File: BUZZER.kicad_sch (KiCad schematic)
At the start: 4 parts, among them Q1 AO3400A, U21 ZX-SH1.0-3PWT

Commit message: update name
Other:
- note removed: "BUZZER"
- company: Pierluigi Colangeli, PhD -> (none)
- title: LEVIA H7 -> (none)

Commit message: upsadte SPI4 set to Baro
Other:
- title: (none) -> H743_ARDUPILOT
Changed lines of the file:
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@@
 	(generator "eeschema")
 	(generator_version "10.0")
-	(paper "A5")
+	(paper "A3")
 	(title_block
+		(title "H743_ARDUPILOT")
 		(date "2026-09-24")
 	)

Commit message: re annotate componant globaly
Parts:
- renumbered R34 to R33, R35 to R34, U21 to U10
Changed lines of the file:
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@@
 		(dnp no)
 		(fields_autoplaced yes)
-		(property "Reference" "#PWR0114"
+		(property "Reference" "#PWR089"
 			(at 135.89 68.58 0)
 			(hide yes)
@@
 			(project "H743_Ardupilot"
 				(path "/6b768b36-fce6-4be0-9021-6d41bddc3a70/40acc3ff-a355-41ce-95b6-fe5d468e4bb9"
-					(reference "#PWR0114")
+					(reference "#PWR089")
 					(unit 1)
 				)
@@
 		(in_pos_files yes)
 		(dnp no)
-		(property "Reference" "R35"
+		(property "Reference" "R34"
 			(at 97.155 64.135 0)
 			(show_name no)
@@
 			(project "H743_Ardupilot"
 				(path "/6b768b36-fce6-4be0-9021-6d41bddc3a70/40acc3ff-a355-41ce-95b6-fe5d468e4bb9"
-					(reference "R35")
+					(reference "R34")
 					(unit 1)
 				)
@@
 		(dnp no)
 		(fields_autoplaced yes)
-		(property "Reference" "#PWR0112"
+		(property "Reference" "#PWR087"
 			(at 104.14 77.47 0)
 			(hide yes)
@@
 			(project "H743_Ardupilot"
 				(path "/6b768b36-fce6-4be0-9021-6d41bddc3a70/40acc3ff-a355-41ce-95b6-fe5d468e4bb9"
-					(reference "#PWR0112")
+					(reference "#PWR087")
 					(unit 1)
 				)
@@
 		(in_pos_files yes)
 		(dnp no)
-		(property "Reference" "R34"
+		(property "Reference" "R33"
 			(at 85.09 60.96 90)
 			(show_name no)
@@
 			(project "H743_Ardupilot"
 				(path "/6b768b36-fce6-4be0-9021-6d41bddc3a70/40acc3ff-a355-41ce-95b6-fe5d468e4bb9"
-					(reference "R34")
+					(reference "R33")
 					(unit 1)
 				)
@@
 		(dnp no)
 		(fields_autoplaced yes)
-		(property "Reference" "#PWR0113"
+		(property "Reference" "#PWR088"
 			(at 133.35 50.8 0)
 			(hide yes)
@@
 			(project "H743_Ardupilot"
 				(path "/6b768b36-fce6-4be0-9021-6d41bddc3a70/40acc3ff-a355-41ce-95b6-fe5d468e4bb9"
-					(reference "#PWR0113")
+					(reference "#PWR088")
 					(unit 1)
 				)
@@
 		(in_pos_files yes)
 		(dnp no)
-		(property "Reference" "U21"
+		(property "Reference" "U10"
 			(at 139.7 45.72 0)
 			(show_name no)
@@
 			(project "H743_Ardupilot"
 				(path "/6b768b36-fce6-4be0-9021-6d41bddc3a70/40acc3ff-a355-41ce-95b6-fe5d468e4bb9"
-					(reference "U21")
+					(reference "U10")
 					(unit 1)
 				)

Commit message: audit DigiKey metadata: BUZZER.kicad_sch
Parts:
- Q1: DigiKey Price Qty (none) -> 1 CT; DigiKey Specs (none) -> N-MOSFET 30 V, 5.7 A, SOT-23-3, RDS(on) 26.5 mΩ max @10 V; DigiKey Status (none) -> Active; DigiKey URL (none) -> https://www.digikey.fr/fr/products/detail/alpha-omega-semic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; DigiKey Unit Price EUR (none) -> 0.45; Footprint Audit (none) -> OK; Library Audit (none) -> KiCad standard; Manufacturer Alpha & Omega Semicon -> Alpha & Omega Semiconductor; Package (none) -> SOT-23-3; Price Checked (none) -> 2026-09-25
- R33: DigiKey Price Qty (none) -> 1 CT; DigiKey Specs (none) -> 1K ±1%, 0402 (1005), thick film; DigiKey Status (none) -> Active / DigiKey family verified; DigiKey URL (none) -> https://www.digikey.fr/en/products/result?keywords=RC0402FR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; DigiKey Unit Price EUR (none) -> 0.09; Footprint Audit (none) -> OK; LCSC C11702 -> (none); LCSC Part C11702 -> (none); Library Audit (none) -> KiCad standard; MPN 0402WGF1001TCE -> RC0402FR-071KL; Manufacturer UNI-ROYAL(Uniroyal Elec) -> YAGEO; Package (none) -> 0402 (1005 Metric); Price Checked (none) -> 2026-09-25
- R34: DigiKey Price Qty (none) -> 1 CT; DigiKey Specs (none) -> 10K ±1%, 0402 (1005), thick film; DigiKey Status (none) -> Active / DigiKey family verified; DigiKey URL (none) -> https://www.digikey.fr/en/products/result?keywords=RC0402FR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; DigiKey Unit Price EUR (none) -> 0.09; Footprint Audit (none) -> OK; LCSC C25744 -> (none); LCSC Part C25744 -> (none); Library Audit (none) -> KiCad standard; MPN 0402WGF1002TCE -> RC0402FR-0710KL; Manufacturer UNI-ROYAL(Uniroyal Elec) -> YAGEO; Package (none) -> 0402 (1005 Metric); Price Checked (none) -> 2026-09-25
- U10: DigiKey Specs (none) -> SH 1.0 mm, 3-pin right-angle SMD; DigiKey Status (none) -> No exact DigiKey listing; supplier/LCSC part retained; Footprint Audit (none) -> CHECK supplier drawing vs EasyEDA footprint; Library Audit (none) -> EasyEDA external; Manufacturer Megastar(兆星) -> Megastar; Package (none) -> SH1.0 3P right-angle SMD; Price Checked (none) -> 2026-09-25

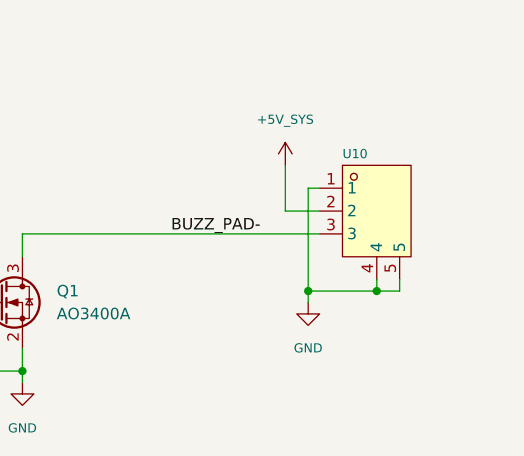
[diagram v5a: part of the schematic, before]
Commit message: add pad for buzzer ouput
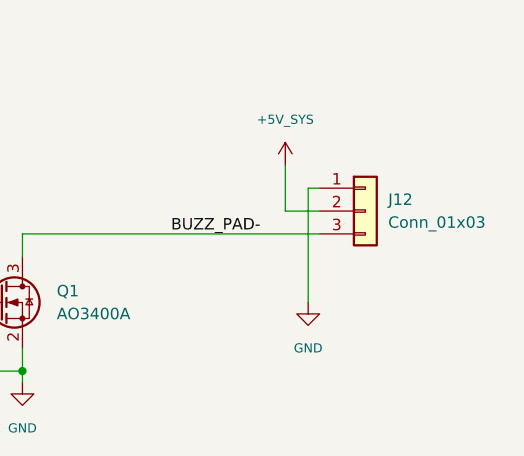
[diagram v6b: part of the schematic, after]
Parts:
- removed U10: ZX-SH1.0-3PWT, EasyEDA:CONN-SMD_3P-P1.00_MEGASTAR_ZX-SH1.0-3PWT, symbol EasyEDA:ZX-SH1.0-3PWT
- added J12: Conn_01x03, symbol Connector_Generic:Conn_01x03
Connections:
- net +5V_SYS: now also J12.2 (Pin_2)
- net BUZZ_PAD-: now also J12.3 (Pin_3)
- net GND: now also J12.1 (Pin_1)
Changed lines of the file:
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@@
 	(generator "eeschema")
 	(generator_version "10.0")
-	(paper "A3")
+	(paper "A4")
 	(title_block
 		(title "H743_ARDUPILOT")
 		(date "2026-09-24")
-	)
-	(junction
-		(at 135.89 60.96)
-		(diameter 0)
-		(color 0 0 0 0)
-	)
-	(junction
-		(at 143.51 60.96)
-		(diameter 0)
-		(color 0 0 0 0)
 	)
 	(junction
@@
 	(wire
 		(pts
-			(xy 143.51 60.96) (xy 146.05 60.96)
-		)
-		(stroke
-			(width 0)
-			(type default)
-		)
-	)
-	(wire
-		(pts
-			(xy 135.89 62.23) (xy 135.89 60.96)
-		)
-		(stroke
-			(width 0)
-			(type default)
-		)
-	)
-	(wire
-		(pts
 			(xy 24.13 33.02) (xy 34.29 33.02)
 		)
@@
 	(wire
 		(pts
-			(xy 143.51 59.69) (xy 143.51 60.96)
-		)
-		(stroke
-			(width 0)
-			(type default)
-		)
-	)
-	(wire
-		(pts
 			(xy 91.44 62.23) (xy 93.98 62.23)
 		)
@@
 	(wire
 		(pts
-			(xy 146.05 60.96) (xy 146.05 59.69)
-		)
-		(stroke
-			(width 0)
-			(type default)
-		)
-	)
-	(wire
-		(pts
 			(xy 135.89 49.53) (xy 137.16 49.53)
 		)
@@
 	(wire
 		(pts
-			(xy 135.89 49.53) (xy 135.89 60.96)
+			(xy 135.89 49.53) (xy 135.89 62.23)
 		)
 		(stroke
@@
 		(pts
 			(xy 93.98 62.23) (xy 93.98 63.5)
-		)
-		(stroke
-			(width 0)
-			(type default)
-		)
-	)
-	(wire
-		(pts
-			(xy 135.89 60.96) (xy 143.51 60.96)
 		)
 		(stroke
@@
 	)
 	(symbol
+		(lib_id "Connector_Generic:Conn_01x03")
+		(at 142.24 52.07 0)
+		(unit 1)
+		(body_style 1)
+		(exclude_from_sim no)
+		(in_bom yes)
+		(on_board yes)
+		(in_pos_files yes)
+		(dnp no)
+		(fields_autoplaced yes)
+		(property "Reference" "J12"
+			(at 144.78 50.7999 0)
+			(show_name no)
+			(do_not_autoplace no)
+			(effects
+				(font
+					(size 1.27 1.27)
+				)
+				(justify left)
+			)
+		)
+		(property "Value" "Conn_01x03"
+			(at 144.78 53.3399 0)
+			(show_name no)
+			(do_not_autoplace no)
+			(effects
+				(font
+					(size 1.27 1.27)
+				)
+				(justify left)
+			)
+		)
+		(property "Footprint" ""
+			(at 142.24 52.07 0)
+			(hide yes)
+			(show_name no)
+			(do_not_autoplace no)
+			(effects
+				(font
+					(size 1.27 1.27)
+				)
+			)
+		)
+		(property "Datasheet" ""
+			(at 142.24 52.07 0)
+			(hide yes)
+			(show_name no)
+			(do_not_autoplace no)
+			(effects
+				(font
+					(size 1.27 1.27)
+				)
+			)
+		)
+		(property "Description" "Generic connector, single row, 01x03, script generated (kicad-library-utils/schlib/autogen/connector/)"
+			(at 142.24 52.07 0)
+			(hide yes)
+			(show_name no)
+			(do_not_autoplace no)
+			(effects
+				(font
+					(size 1.27 1.27)
+				)
+			)
+		)
+		(pin "1"
+		)
+		(pin "2"
+		)
+		(pin "3"
+		)
+		(instances
+			(project "H743_Ardupilot"
+				(path "/6b768b36-fce6-4be0-9021-6d41bddc3a70/40acc3ff-a355-41ce-95b6-fe5d468e4bb9"
+					(reference "J12")
+					(unit 1)
+				)
+			)
+		)
+	)
+	(symbol
 		(lib_id "power:GND")
 		(at 104.14 71.12 0)
@@
 					(unit 1)
 				)
-			)
-		)
-	)
-	(symbol
-		(lib_id "EasyEDA:ZX-SH1.0-3PWT")
-		(at 142.24 52.07 0)
-		(unit 1)
-		(body_style 1)
-		(exclude_from_sim no)
-		(in_bom yes)
-		(on_board yes)
-		(in_pos_files yes)
-		(dnp no)
-		(property "Reference" "U10"
-			(at 139.7 45.72 0)
-			(show_name no)
-			(do_not_autoplace no)
-			(effects
-				(font
-					(size 1.016 1.016)
-				)
-				(justify left)
-			)
-		)
-		(property "Value" "ZX-SH1.0-3PWT"
-			(at 148.59 53.3399 0)
-			(hide yes)
-			(show_name no)
-			(do_not_autoplace no)
-			(effects
-				(font
-					(size 1.016 1.016)
-				)
-				(justify left)
-			)
-		)
-		(property "Footprint" "EasyEDA:CONN-SMD_3P-P1.00_MEGASTAR_ZX-SH1.0-3PWT"
-			(at 142.24 67.31 0)
-			(hide yes)
-			(show_name no)
-			(do_not_autoplace no)
-			(effects
-				(font
-					(size 1.27 1.27)
-				)
-			)
-		)
-		(property "Datasheet" "https://www.lcsc.com/datasheet/C7430445.pdf"
-			(at 142.24 69.85 0)
-			(hide yes)
-			(show_name no)
-			(do_not_autoplace no)
-			(effects
-				(font
-					(size 1.27 1.27)
-				)
-			)
-		)
-		(property "Description" ""
-			(at 142.24 52.07 0)
-			(hide yes)
-			(show_name no)
-			(do_not_autoplace no)
-			(effects
-				(font
-					(size 1.27 1.27)
-				)
-			)
-		)
-		(property "Manufacturer" "Megastar"
-			(at 142.24 72.39 0)
-			(hide yes)
-			(show_name no)
-			(do_not_autoplace no)
-			(effects
-				(font
-					(size 1.27 1.27)
-				)
-			)
-		)
-		(property "MPN" "ZX-SH1.0-3PWT"
-			(at 142.24 74.93 0)
-			(hide yes)
-			(show_name no)
-			(do_not_autoplace no)
-			(effects
-				(font
-					(size 1.27 1.27)
-				)
-			)
-		)
-		(property "LCSC Part" "C7430445"
-			(at 142.24 77.47 0)
-			(hide yes)
-			(show_name no)
-			(do_not_autoplace no)
-			(effects
-				(font
-					(size 1.27 1.27)
-				)
-			)
-		)
-		(property "LCSC" "C7430445"
-			(at 142.24 52.07 0)
-			(hide yes)
-			(show_name no)
-			(do_not_autoplace no)
-			(effects
-				(font
-					(size 1.27 1.27)
-				)
-			)
-		)
-		(property "DigiKey URL" ""
-			(at 139.7 45.72 0)
-			(hide yes)
-			(show_name no)
-			(do_not_autoplace no)
-			(effects
-				(font
-					(size 1.27 1.27)
-				)
-			)
-		)
-		(property "DigiKey Specs" "SH 1.0 mm, 3-pin right-angle SMD"
-			(at 139.7 45.72 0)
-			(hide yes)
-			(show_name no)
-			(do_not_autoplace no)
-			(effects
-				(font
-					(size 1.27 1.27)
-				)
-			)
-		)
-		(property "DigiKey Unit Price EUR" ""
-			(at 139.7 45.72 0)
-			(hide yes)
-			(show_name no)
-			(do_not_autoplace no)
-			(effects
-				(font
-					(size 1.27 1.27)
-				)
-			)
-		)
-		(property "DigiKey Price Qty" ""
-			(at 139.7 45.72 0)
-			(hide yes)
-			(show_name no)
-			(do_not_autoplace no)
-			(effects
-				(font
-					(size 1.27 1.27)
-				)
-			)
-		)
-		(property "Price Checked" "2026-09-25"
-			(at 139.7 45.72 0)
-			(hide yes)
-			(show_name no)
-			(do_not_autoplace no)
-			(effects
-				(font
-					(size 1.27 1.27)
-				)
-			)
-		)
-		(property "DigiKey Status" "No exact DigiKey listing; supplier/LCSC part retained"
-			(at 139.7 45.72 0)
-			(hide yes)
-			(show_name no)
-			(do_not_autoplace no)
-			(effects
-				(font
-					(size 1.27 1.27)
-				)
-			)
-		)
-		(property "Package" "SH1.0 3P right-angle SMD"
-			(at 139.7 45.72 0)
-			(hide yes)
-			(show_name no)
-			(do_not_autoplace no)
-			(effects
-				(font
-					(size 1.27 1.27)
-				)
-			)
-		)
-		(property "Footprint Audit" "CHECK supplier drawing vs EasyEDA footprint"
-			(at 139.7 45.72 0)
-			(hide yes)
-			(show_name no)
-			(do_not_autoplace no)
-			(effects
-				(font
-					(size 1.27 1.27)
-				)
-			)
-		)
-		(property "Library Audit" "EasyEDA external"
-			(at 139.7 45.72 0)
-			(hide yes)
-			(show_name no)
-			(do_not_autoplace no)
-			(effects
-				(font
-					(size 1.27 1.27)
-				)
-			)
-		)
-		(pin "1"
-		)
-		(pin "3"
-		)
-		(pin "4"
-		)
-		(pin "5"
-		)
-		(pin "2"
-		)
-		(instances
-			(project "H743_Ardupilot"
-				(path "/6b768b36-fce6-4be0-9021-6d41bddc3a70/40acc3ff-a355-41ce-95b6-fe5d468e4bb9"
-					(reference "U10")
-					(unit 1)
-				)

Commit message: assign Matek-style solder pad footprints in BUZZER.kicad_sch
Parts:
- J12: footprint (none) -> H743_Custom:SolderPadArray_1x03_P2.54mm_1x1mm
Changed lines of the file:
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@@
 			)
 		)
-		(property "Footprint" ""
+		(property "Footprint" "H743_Custom:SolderPadArray_1x03_P2.54mm_1x1mm"
 			(at 142.24 52.07 0)
 			(hide yes)

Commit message: update
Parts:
- renumbered J12 to J10, R33 to R39, R34 to R40
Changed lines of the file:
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@@
 		(dnp no)
 		(fields_autoplaced yes)
-		(property "Reference" "#PWR089"
+		(property "Reference" "#PWR0118"
 			(at 135.89 68.58 0)
 			(hide yes)
@@
 			(project "H743_Ardupilot"
 				(path "/6b768b36-fce6-4be0-9021-6d41bddc3a70/40acc3ff-a355-41ce-95b6-fe5d468e4bb9"
-					(reference "#PWR089")
+					(reference "#PWR0118")
 					(unit 1)
 				)
@@
 		(in_pos_files yes)
 		(dnp no)
-		(property "Reference" "R34"
+		(property "Reference" "R40"
 			(at 97.155 64.135 0)
 			(show_name no)
@@
 			(project "H743_Ardupilot"
 				(path "/6b768b36-fce6-4be0-9021-6d41bddc3a70/40acc3ff-a355-41ce-95b6-fe5d468e4bb9"
-					(reference "R34")
+					(reference "R40")
 					(unit 1)
 				)
@@
 		(dnp no)
 		(fields_autoplaced yes)
-		(property "Reference" "J12"
+		(property "Reference" "J10"
 			(at 144.78 50.7999 0)
 			(show_name no)
@@
 			(project "H743_Ardupilot"
 				(path "/6b768b36-fce6-4be0-9021-6d41bddc3a70/40acc3ff-a355-41ce-95b6-fe5d468e4bb9"
-					(reference "J12")
+					(reference "J10")
 					(unit 1)
 				)
@@
 		(dnp no)
 		(fields_autoplaced yes)
-		(property "Reference" "#PWR087"
+		(property "Reference" "#PWR0116"
 			(at 104.14 77.47 0)
 			(hide yes)
@@
 			(project "H743_Ardupilot"
 				(path "/6b768b36-fce6-4be0-9021-6d41bddc3a70/40acc3ff-a355-41ce-95b6-fe5d468e4bb9"
-					(reference "#PWR087")
+					(reference "#PWR0116")
 					(unit 1)
 				)
@@
 		(in_pos_files yes)
 		(dnp no)
-		(property "Reference" "R33"
+		(property "Reference" "R39"
 			(at 85.09 60.96 90)
 			(show_name no)
@@
 			(project "H743_Ardupilot"
 				(path "/6b768b36-fce6-4be0-9021-6d41bddc3a70/40acc3ff-a355-41ce-95b6-fe5d468e4bb9"
-					(reference "R33")
+					(reference "R39")
 					(unit 1)
 				)
@@
 		(dnp no)
 		(fields_autoplaced yes)
-		(property "Reference" "#PWR088"
+		(property "Reference" "#PWR0117"
 			(at 133.35 50.8 0)
 			(hide yes)
@@
 			(project "H743_Ardupilot"
 				(path "/6b768b36-fce6-4be0-9021-6d41bddc3a70/40acc3ff-a355-41ce-95b6-fe5d468e4bb9"
-					(reference "#PWR088")
+					(reference "#PWR0117")
 					(unit 1)
 				)
